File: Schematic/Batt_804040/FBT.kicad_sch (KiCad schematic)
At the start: 16 parts, among them J1 TRRS Connector 3.5, J2 Conn_01x04, SW1 SW_SPDT

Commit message: Work on silkscreen logo
Made a mascot, "Mr. Tracker" which looks a lot like Mr. Lunt mixed with Pa Grape.
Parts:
- removed J2: Conn_01x04, Connector_JST:JST_PH_S4B-PH-K_1x04_P2.00mm_Horizontal, symbol Connector_Generic:Conn_01x04
- added J2: TRRS Connector 3.5, My_Library:PJ-320A, symbol Connector_Audio:AudioJack4
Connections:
- net ESP32_3V3: now also J2.T
- net GND: now also J2.S
- net SCL_1: now also J2.R2
- net SDA_1: now also J2.R1
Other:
- moved on the sheet: J1, MCU1

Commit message: work on PCBs, logos, and case
did more work on 18650 battery model
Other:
- note added: "The GY-27X must be connected to the BMI's 3v3 output so that its logic levels are 3v3. Connecting it to 5v is OK for the GY-273, but the GY-271 will alter i2c logic levels to output 5V, which may hurt the BMI160 Depending on the IMU board, it may not have a 5v tolerant input and instead may need to tap into the 3v3 one. I made the 3v3 input the default one for the sake of versatility."
- note removed: "The GY-27X must be connected to the BMI's 3v3 output so that its logic levels are 3v3. Connecting it to 5v is OK for the GY-273, but the GY-271 will alter i2c logic levels to output 5V, which may hurt the BMI160 Depending on the IMU board, it may not have a 5v tolerant input and instead may need to tap into the 3v3 one."
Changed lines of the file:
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@@
 		)
 	)
-	(text "The GY-27X must be connected to the BMI's 3v3 output so that its logic levels are 3v3.\nConnecting it to 5v is OK for the GY-273, but the GY-271 will alter i2c logic levels to output 5V,\nwhich may hurt the BMI160\n\nDepending on the IMU board, it may not have a\n5v tolerant input and instead may need to tap into the 3v3 one."
+	(text "The GY-27X must be connected to the BMI's 3v3 output so that its logic levels are 3v3.\nConnecting it to 5v is OK for the GY-273, but the GY-271 will alter i2c logic levels to output 5V,\nwhich may hurt the BMI160\n\nDepending on the IMU board, it may not have a\n5v tolerant input and instead may need to tap into the 3v3 one.\nI made the 3v3 input the default one for the sake of versatility."
 		(exclude_from_sim no)
-		(at 185.674 20.32 0)
+		(at 185.166 21.082 0)
 		(effects
 			(font

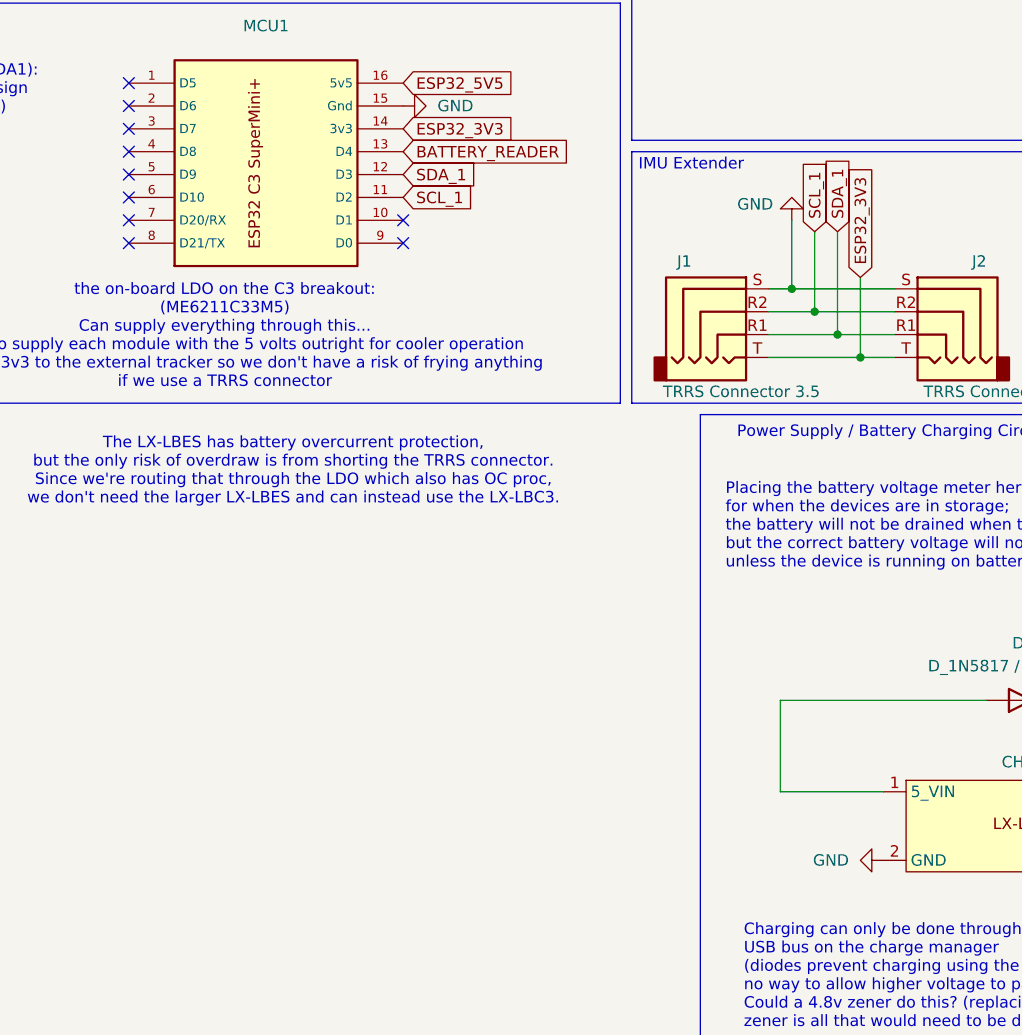
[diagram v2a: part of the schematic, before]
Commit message: Rework MrTracker footprint to support the big lx-lbes
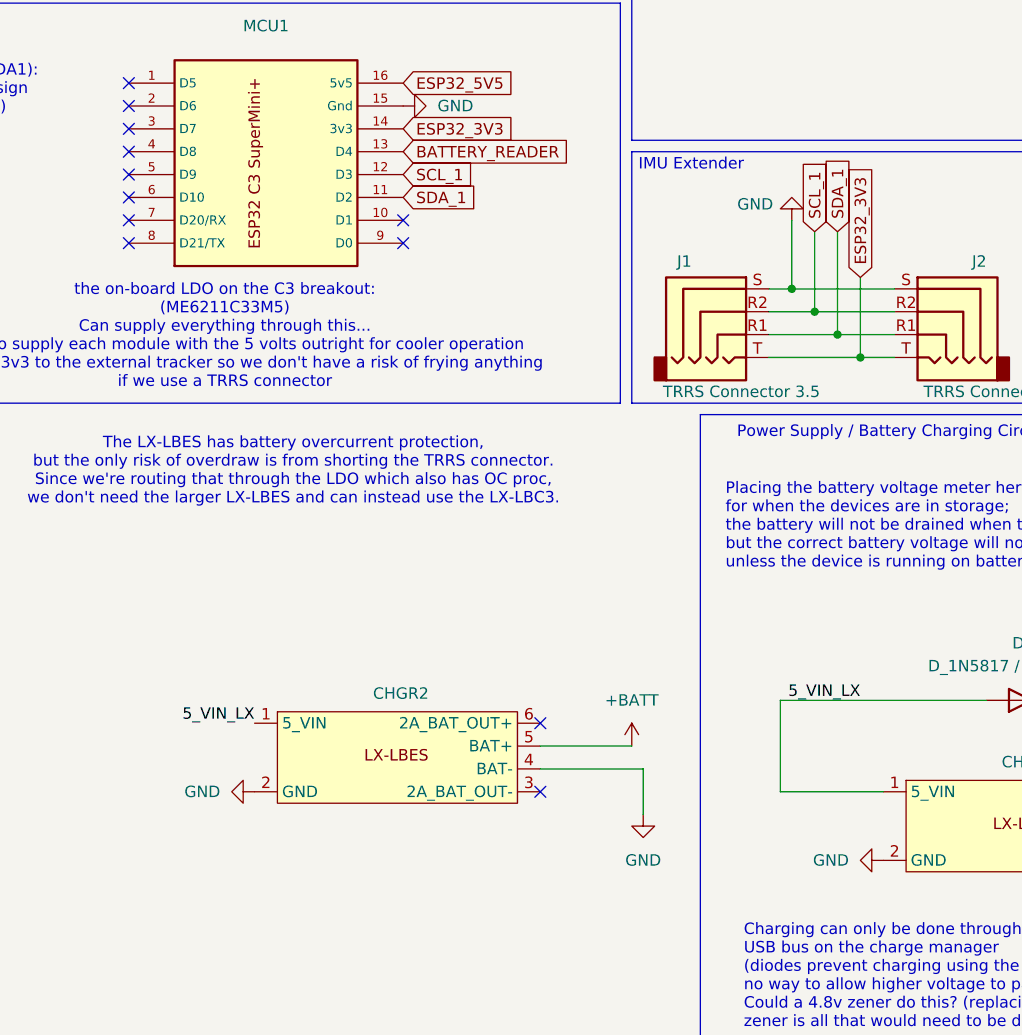
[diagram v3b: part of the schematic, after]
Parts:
- added CHGR2: ~, My_Library:LX-LBES-Big, symbol My_Library:LX-LBES
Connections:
- net +BATT: now also CHGR2.5 (BAT+)
- net GND: now also CHGR2.2 (GND), CHGR2.4 (BAT-)
- net SCL_1: now also MCU1.12 (D3); no longer MCU1.11 (D2)
- net SDA_1: now also MCU1.11 (D2); no longer MCU1.12 (D3)
- net 5_VIN_LX: now reaches CHGR1.1 (5_VIN), D1.2 (A)
- net 5_VIN_LX: now also CHGR2.1 (5_VIN)
- no-connect marks 25 -> 27

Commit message: prep v2 PCB for production
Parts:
- MCU1: footprint Espressif:ESP32-C3-SuperMini_PLUS -> Espressif:ESP32-C3-Mini-V1
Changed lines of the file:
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@@
 			)
 		)
-		(property "Footprint" "Espressif:ESP32-C3-SuperMini_PLUS"
+		(property "Footprint" "Espressif:ESP32-C3-Mini-V1"
 			(at 124.46 46.99 0)
 			(effects

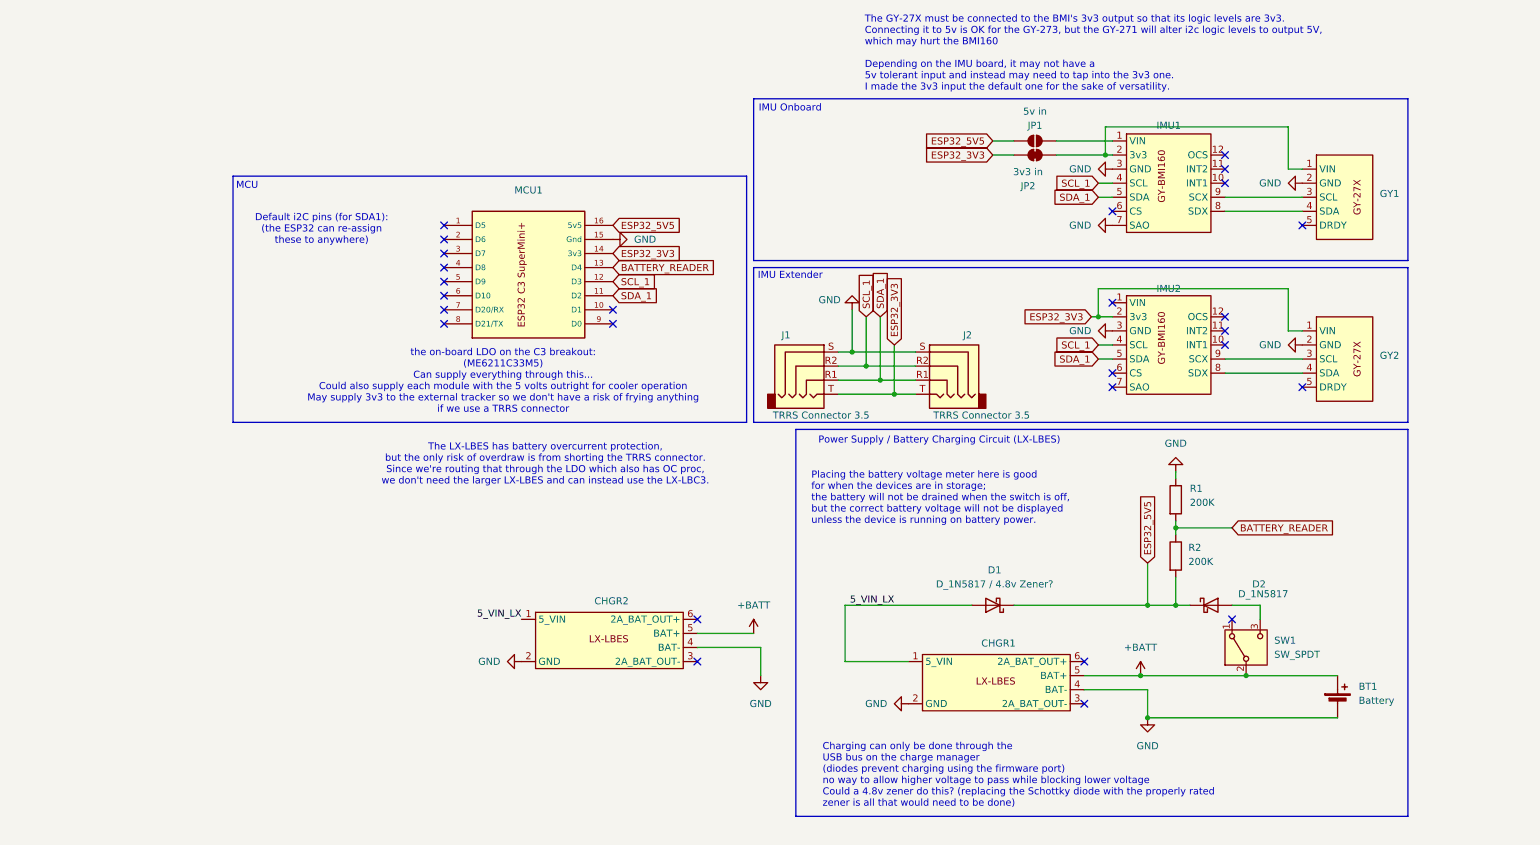
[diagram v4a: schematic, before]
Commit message: Start editing schematic for better power supply
removed diodes and experimenting with multiple LDOs for supplying power from all inputs
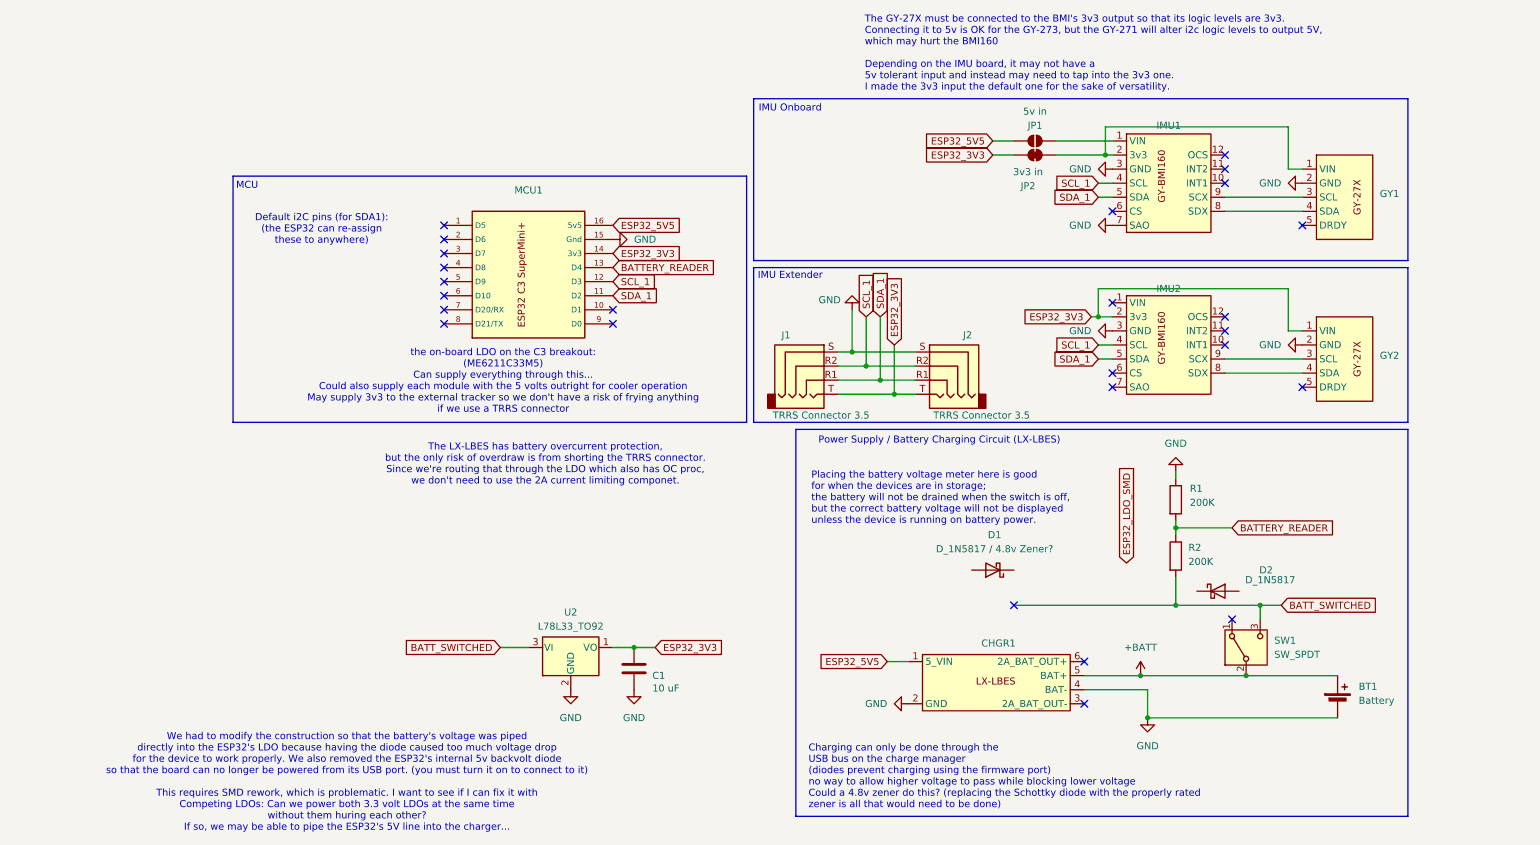
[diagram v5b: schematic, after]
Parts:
- removed CHGR2: ~, My_Library:LX-LBES-Big, symbol My_Library:LX-LBES
- added C1: 10 uF, symbol Device:C
- added U2: L78L33_TO92, Package_TO_SOT_THT:TO-92L_HandSolder, symbol Regulator_Linear:L78L33_TO92
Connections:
- net ESP32_3V3: now also C1.1, U2.1 (VO)
- net ESP32_5V5: now also CHGR1.1 (5_VIN); no longer D1.1 (K), D2.1 (K), R2.2
- net GND: now also C1.2, U2.2 (GND)
- net at D2.2 (A): no longer SW1.3 (C)
- net 5_VIN_LX: no longer names the net of D1.2 (A)
- net 5_VIN_LX: no longer CHGR1.1 (5_VIN)
- new net BATT_SWITCHED: R2.2, SW1.3 (C), U2.3 (VI)
- no-connect marks 27 -> 26
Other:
- note added: "The LX-LBES has battery overcurrent protection, but the only risk of overdraw is from shorting the TRRS connector. Since we're routing that through the LDO which also has OC proc, we don't need to use the 2A current limiting componet."
- note added: "We had to modify the construction so that the battery's voltage was piped directly into the ESP32's LDO because having the diode caused too much voltage drop for the device to work properly. We also removed the ESP32's internal 5v backvolt diode so that the board can no longer be powered from its USB port. (you must turn it on to connect to it) This requires SMD rework, which is problematic. I wa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"
- note removed: "The LX-LBES has battery overcurrent protection, but the only risk of overdraw is from shorting the TRRS connector. Since we're routing that through the LDO which also has OC proc, we don't need the larger LX-LBES and can instead use the LX-LBC3."
- moved on the sheet: D1, D2

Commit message: Update schematic to v3
Added support for a discrete LDO (HT7333) so we can correct the bodge we did with the original design.
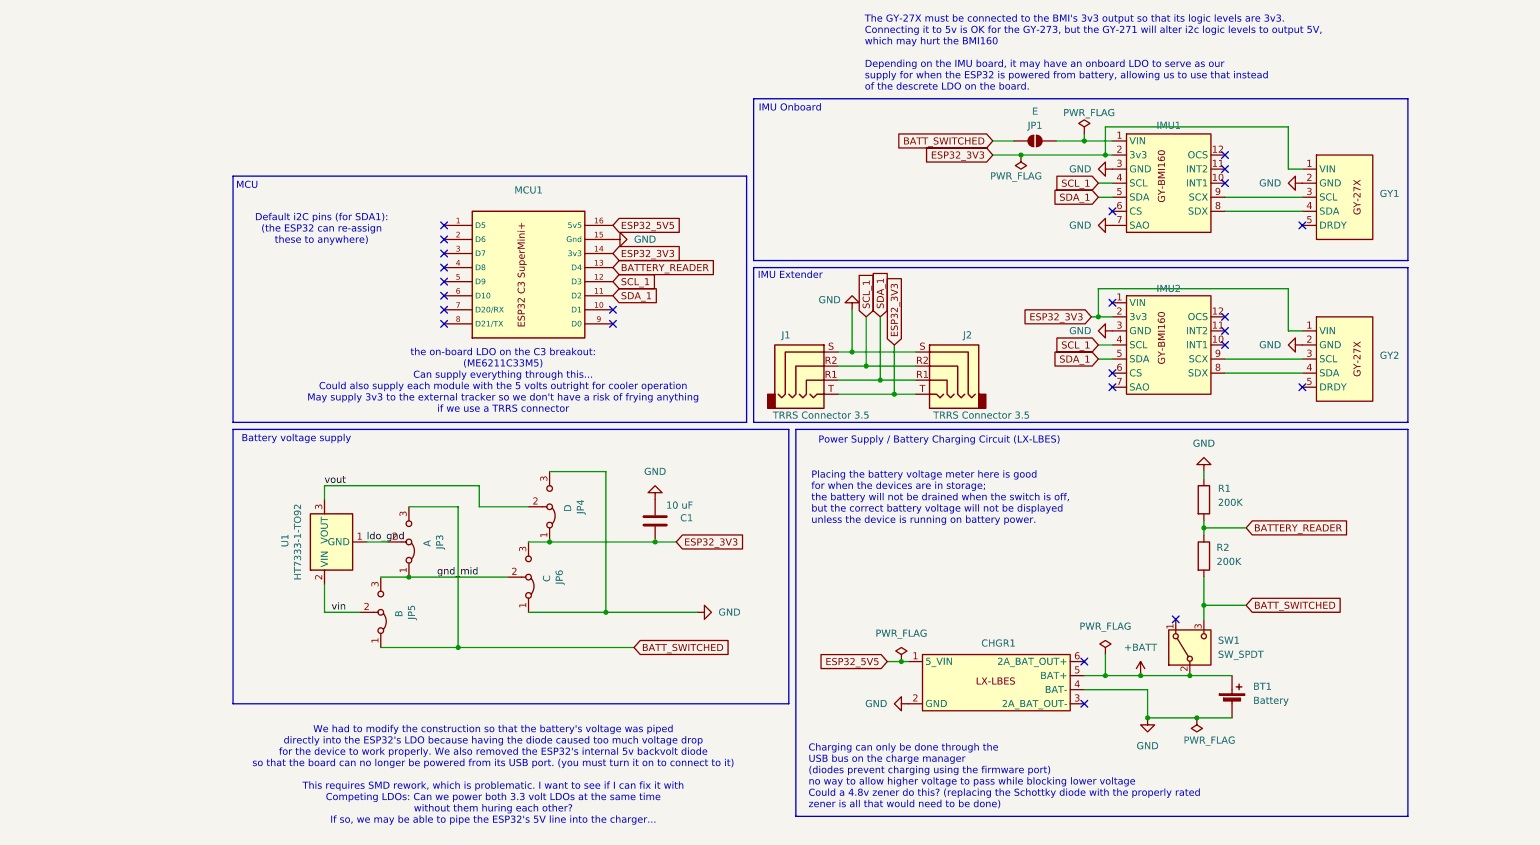
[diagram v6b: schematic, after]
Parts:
- removed D1: D_1N5817 / 4.8v Zener?, Diode_THT:D_DO-41_SOD81_P7.62mm_Horizontal, symbol Device:D_Schottky
- removed D2: D_1N5817, Diode_THT:D_DO-41_SOD81_P7.62mm_Horizontal, symbol Device:D_Schottky
- removed JP2: 3v3 in, Jumper:SolderJumper-2_P1.3mm_Bridged_RoundedPad1.0x1.5mm, symbol Jumper:SolderJumper_2_Bridged
- removed U2: L78L33_TO92, Package_TO_SOT_THT:TO-92L_HandSolder, symbol Regulator_Linear:L78L33_TO92
- added JP3: A, Jumper:SolderJumper-3_P1.3mm_Bridged12_RoundedPad1.0x1.5mm_NumberLabels, symbol Jumper:Jumper_3_Bridged12
- added JP4: D, Jumper:SolderJumper-3_P1.3mm_Bridged12_RoundedPad1.0x1.5mm_NumberLabels, symbol Jumper:Jumper_3_Bridged12
- added JP5: B, Jumper:SolderJumper-3_P1.3mm_Bridged12_RoundedPad1.0x1.5mm_NumberLabels, symbol Jumper:Jumper_3_Bridged12
- added JP6: C, Jumper:SolderJumper-3_P1.3mm_Bridged12_RoundedPad1.0x1.5mm_NumberLabels, symbol Jumper:Jumper_3_Bridged12
- added U1: HT7333-1-TO92, Package_TO_SOT_THT:TO-92L_Inline, symbol Regulator_Linear:HT75xx-1-SOT89
- C1: footprint (none) -> Capacitor_THT:C_Disc_D5.0mm_W2.5mm_P5.00mm
- JP1: value 5v in -> E
- MCU1: footprint Espressif:ESP32-C3-Mini-V1 -> Espressif:ESP32-C3-SuperMini_PLUS
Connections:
- net BATT_SWITCHED: now also JP1.2 (B), JP3.3 (B), JP5.1 (A)
- net ESP32_3V3: now also GY1.1 (VIN), IMU1.2 (3v3), JP4.1 (A), JP6.3 (B)
- net ESP32_5V5: no longer JP1.2 (B)
- net GND: now also JP4.3 (B), JP6.1 (A)
- new net gnd_mid: JP3.1 (A), JP5.3 (B), JP6.2 (C)
- new net ldo_gnd: JP3.2 (C), U1.1 (GND)
- new net vin: JP5.2 (C), U1.2 (VIN)
- new net vout: JP4.2 (C), U1.3 (VOUT)
- no-connect marks 26 -> 25
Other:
- note added: "Battery voltage supply"
- note added: "The GY-27X must be connected to the BMI's 3v3 output so that its logic levels are 3v3. Connecting it to 5v is OK for the GY-273, but the GY-271 will alter i2c logic levels to output 5V, which may hurt the BMI160 Depending on the IMU board, it may have an onboard LDO to serve as our supply for when the ESP32 is powered from battery, allowing us to use that instead of the descrete LDO on the board."
- note removed: "The GY-27X must be connected to the BMI's 3v3 output so that its logic levels are 3v3. Connecting it to 5v is OK for the GY-273, but the GY-271 will alter i2c logic levels to output 5V, which may hurt the BMI160 Depending on the IMU board, it may not have a 5v tolerant input and instead may need to tap into the 3v3 one. I made the 3v3 input the default one for the sake of versatility."
- note removed: "The LX-LBES has battery overcurrent protection, but the only risk of overdraw is from shorting the TRRS connector. Since we're routing that through the LDO which also has OC proc, we don't need to use the 2A current limiting componet."
- moved on the sheet: BT1, C1, R1, R2, SW1
